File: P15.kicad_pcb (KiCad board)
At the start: 2 copper layers, 100.2 x 71.7 mm, 37 parts, among them J1 Screw_Terminal_01x02, J2 Barrel_Jack, J21 Conn_01x16, J3 Slot: Booster, J4 Slot-a1, J6 Screw_Terminal_01x04, J7 Slot: Master, Q1 BC847, U5 L78M12

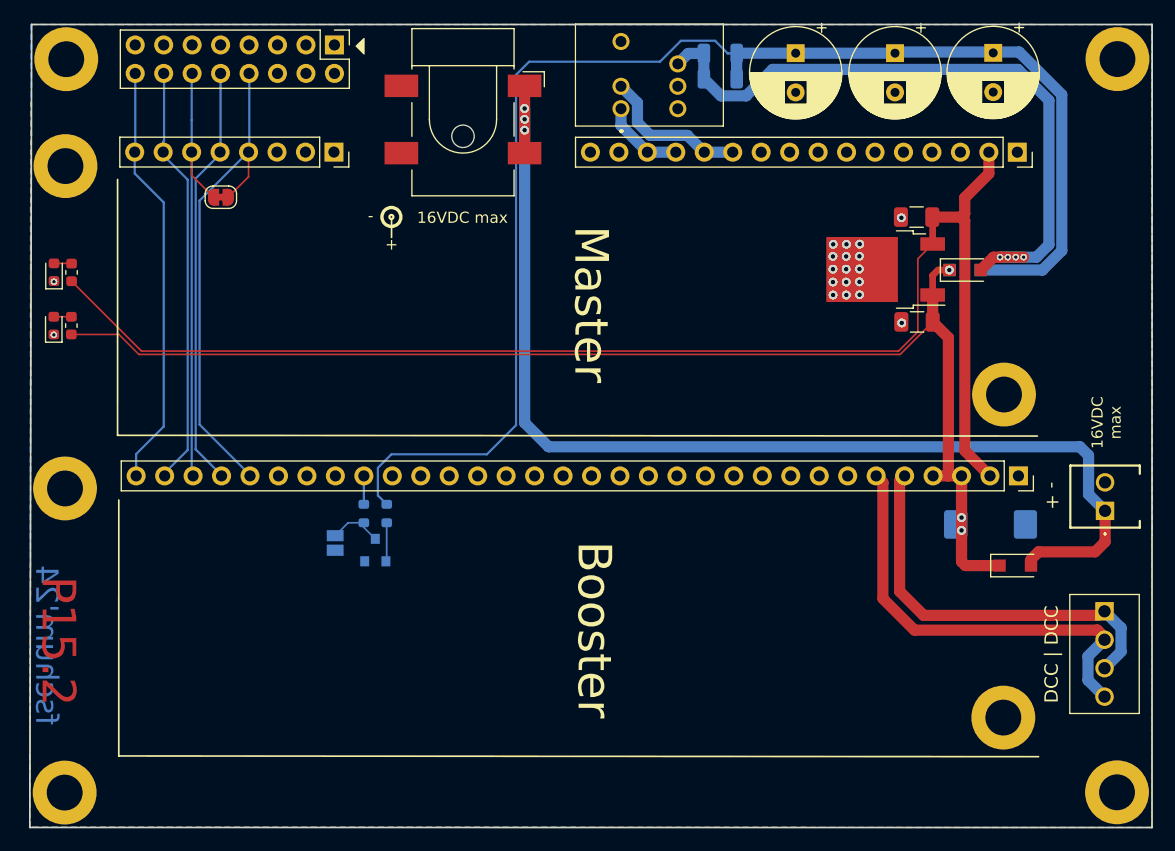
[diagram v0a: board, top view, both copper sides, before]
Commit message: mod: optimized for PCB assembly
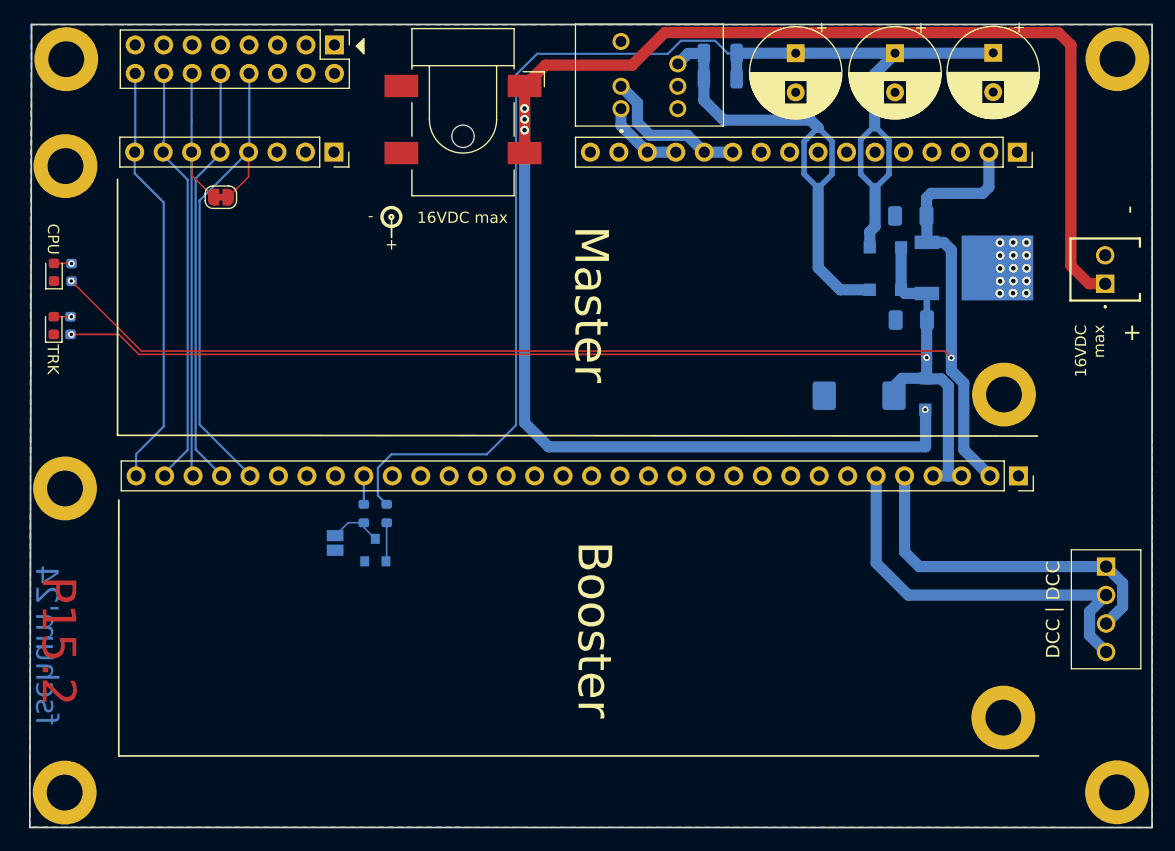
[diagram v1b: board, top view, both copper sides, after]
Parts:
- removed J2: Barrel_Jack, Connector_BarrelJack:BarrelJack_CLIFF_FC681465S_SMT_Horizontal
- added J5: Barrel_Jack_Switch, Connector_BarrelJack:BarrelJack_CLIFF_FC681465S_SMT_Horizontal, F.Cu at (88.7, -61.9)
- C26, C27, D1, D2, R89, R90, U5: moved to B.Cu
- moved J1 20.3 mm to (146.0, -47.2)
- moved D1 17.3 mm to (129.9, -37.4), turned to 270 degrees
- moved C15 16.4 mm to (124.0, -37.2), turned to 180 degrees
- moved U5 7.89 mm to (134.3, -48.6), turned to 0 degrees
- moved D3 7.39 mm to (126.4, -50.4), turned to 180 degrees
- moved D2 7.32 mm to (126.4, -46.6), turned to 180 degrees
- moved J6 3.99 mm to (146.1, -21.9)
- moved C27 0.54 mm to (128.7, -44.0)
- moved C26 0.53 mm to (128.7, -53.2)
- moved R89 0.08 mm to (53.7, -43.5)
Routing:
- net Vsrc: track 101.7 -> 148.7 mm, vias 3 -> 4
- net Net-(D2-Pad2): track 60.5 -> 43.5 mm, vias 4 -> 0
- net Vbst.0: track 112.9 -> 107.1 mm, vias 3 -> 2
- net Vrail: track 123.2 -> 118.6 mm, vias 0 -> 2
- net DCC-1a': track 36.2 -> 31.6 mm
- net Net-(C2-Pad1): track 124.8 -> 121.2 mm
- net DCC-1b': track 38.7 -> 35.8 mm
- net Net-(D25-Pad2): vias 0 -> 1
- net Net-(D14-Pad2): vias 0 -> 1
- net GND: vias 19 -> 15
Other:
- board text added: "CPU"
- board text added: "TRK"
- board text removed: "- +"

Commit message: upgrade to Kicad 9
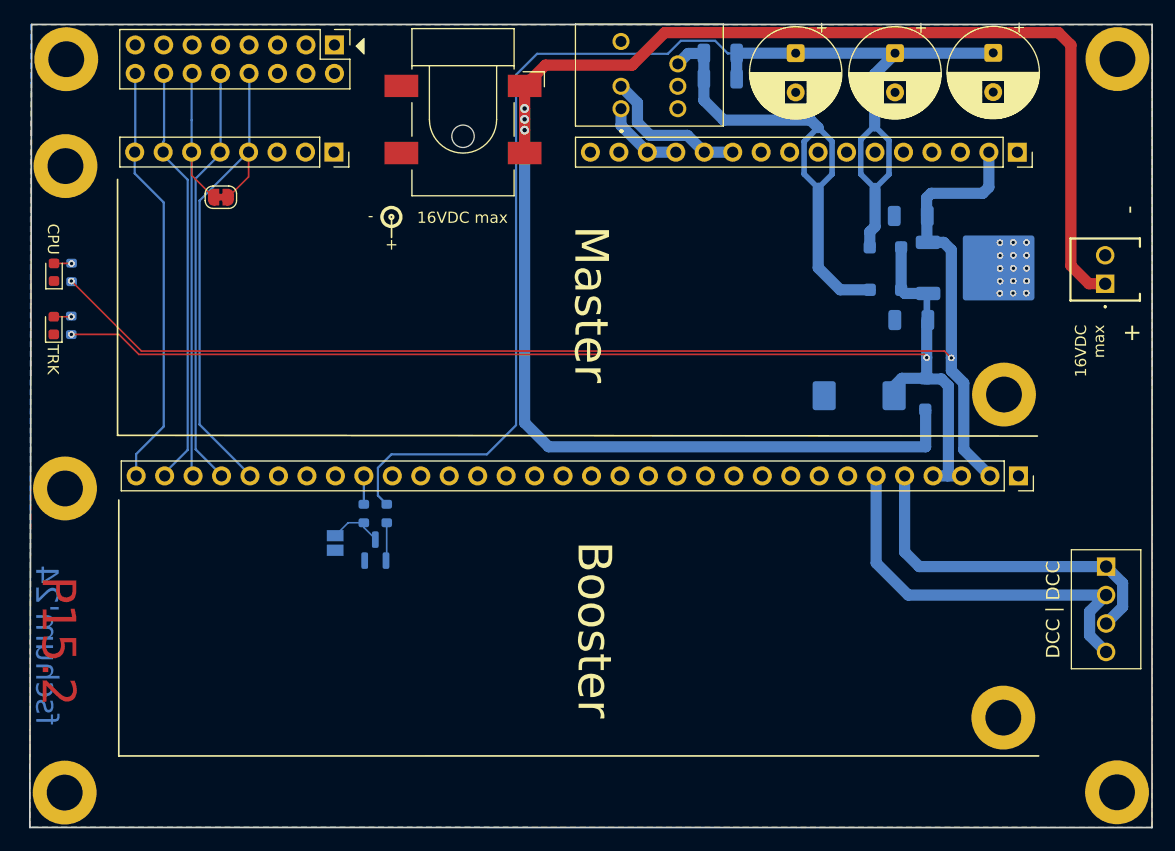
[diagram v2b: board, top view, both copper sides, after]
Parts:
- C27: value 2.2u/35V -> 2.2u/25V
- C3: value 3x 680u/20V -> 680u/20V
- D25: value LED(ylw) -> LED(grn)
- R1, R2: value 68 -> 100
- R89: value 10K -> 22k
- moved U5 0.94 mm to (135.2, -48.6)
- moved R89 0.07 mm to (53.7, -43.5)
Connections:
- net ~BUS.bsi renamed ~{BUS.bsi}
- net ~BUS.bso renamed ~{BUS.bso}
- net ~BUS.rts renamed ~{BUS.rts}
- J21 pad 1: (no net) -> unconnected-(J21-Pin_1-Pad1)
- J21 pad 2: (no net) -> unconnected-(J21-Pin_2-Pad2)
- J21 pad 4: (no net) -> +3V3
- J21 pad 6: (no net) -> unconnected-(J21-Pin_6-Pad6)
- J3 pad 1: (no net) -> unconnected-(J3-Pin_1-Pad1)
- J3 pad 10: (no net) -> unconnected-(J3-Pin_10-Pad10)
- J3 pad 11: (no net) -> unconnected-(J3-Pin_11-Pad11)
- J3 pad 12: (no net) -> unconnected-(J3-Pin_12-Pad12)
- J3 pad 13: (no net) -> unconnected-(J3-Pin_13-Pad13)
- J3 pad 14: (no net) -> unconnected-(J3-Pin_14-Pad14)
- J3 pad 19: (no net) -> unconnected-(J3-Pin_19-Pad19)
- J3 pad 20: (no net) -> unconnected-(J3-Pin_20-Pad20)
- J3 pad 21: (no net) -> unconnected-(J3-Pin_21-Pad21)
- J3 pad 22: (no net) -> unconnected-(J3-Pin_22-Pad22)
- J3 pad 23: (no net) -> unconnected-(J3-Pin_23-Pad23)
- J3 pad 25: (no net) -> SLT1.rx
- J3 pad 26: (no net) -> SLT1.tx
- J3 pad 27: (no net) -> ~{RESET.1}
- J3 pad 7: (no net) -> unconnected-(J3-Pin_7-Pad7)
- J3 pad 8: (no net) -> unconnected-(J3-Pin_8-Pad8)
- J3 pad 9: (no net) -> unconnected-(J3-Pin_9-Pad9)
- J4 pad 1: (no net) -> SLT0.rx
- J4 pad 2: (no net) -> SLT0.tx
- J4 pad 3: (no net) -> ~{RESET.0}
- J7 pad 1: (no net) -> unconnected-(J7-Pin_1-Pad1)
- J7 pad 10: (no net) -> unconnected-(J7-Pin_10-Pad10)
- J7 pad 3: (no net) -> unconnected-(J7-Pin_3-Pad3)
- J7 pad 4: (no net) -> unconnected-(J7-Pin_4-Pad4)
- J7 pad 5: (no net) -> unconnected-(J7-Pin_5-Pad5)
- J7 pad 6: (no net) -> unconnected-(J7-Pin_6-Pad6)
- J7 pad 7: (no net) -> unconnected-(J7-Pin_7-Pad7)
- J7 pad 8: (no net) -> unconnected-(J7-Pin_8-Pad8)
- J7 pad 9: (no net) -> unconnected-(J7-Pin_9-Pad9)
- PS1 pad 4: (no net) -> unconnected-(PS1-ON/OFF-Pad4)
- PS1 pad 5: (no net) -> unconnected-(PS1-NC-Pad5)
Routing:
- net Vsrc: vias 4 -> 3
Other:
- net class Default removed
- net class Power removed
